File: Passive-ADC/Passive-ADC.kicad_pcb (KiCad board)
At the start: 4 copper layers, 24.2 x 16.8 mm, 13 parts, among them J1 FPGA Terminal, J2 ADC Terminal

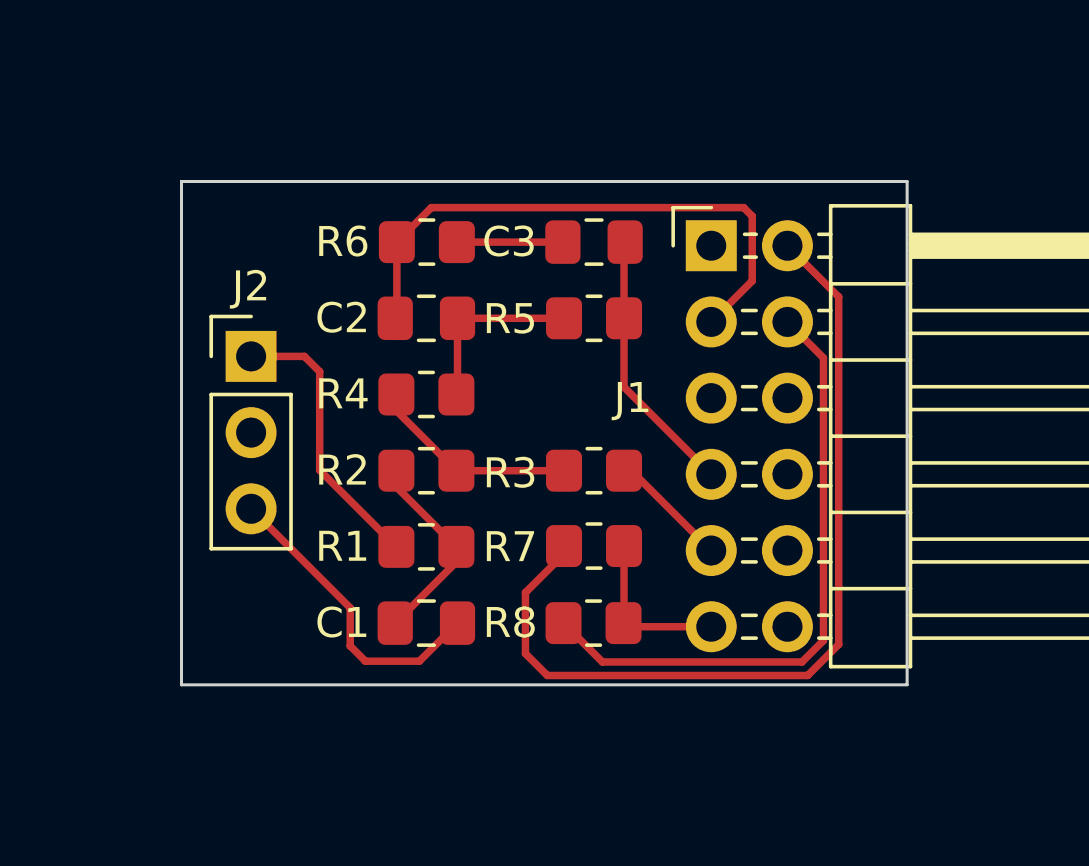
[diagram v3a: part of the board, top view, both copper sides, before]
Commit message: Updated models with new schematic details
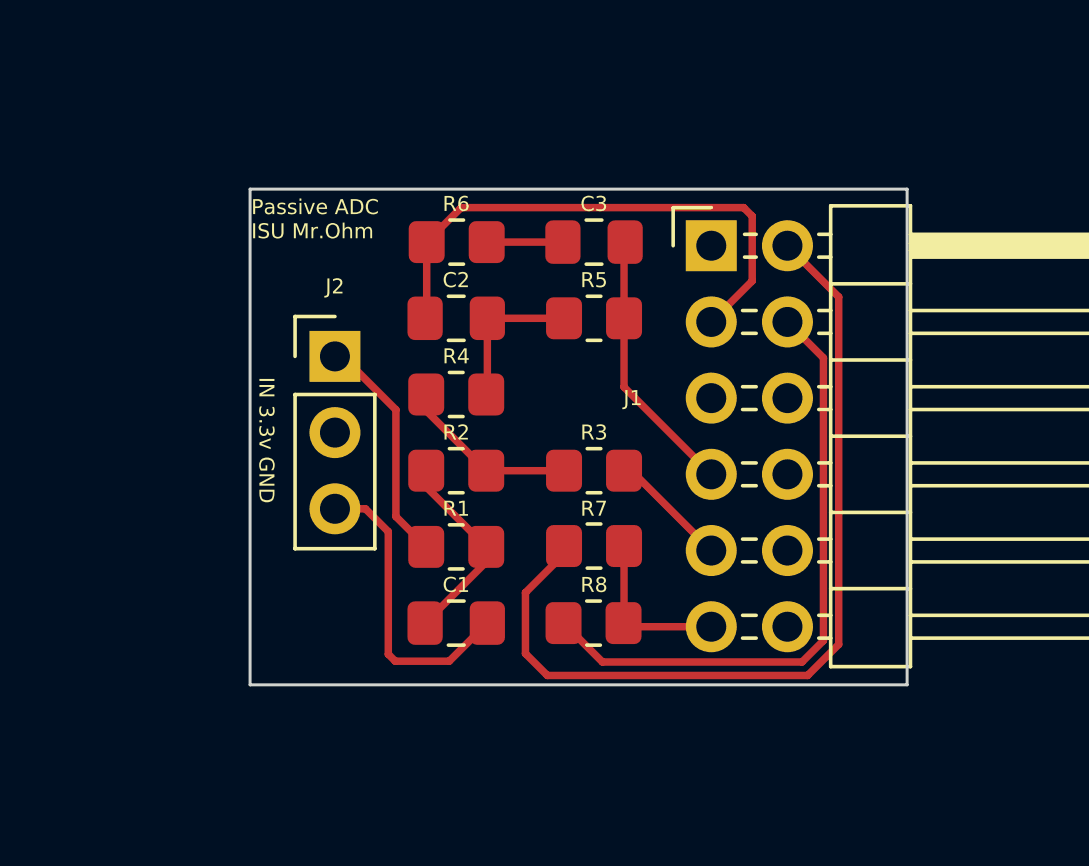
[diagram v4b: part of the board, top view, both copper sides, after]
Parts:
- moved J2 2.79 mm to (144.0, 80.5)
- moved R6 0.99 mm to (148.1, 76.7)
- moved C1 0.99 mm to (148.1, 89.4)
- moved C2 0.99 mm to (148.1, 79.2)
- moved R1 0.99 mm to (148.1, 86.9)
- moved R2 0.99 mm to (148.1, 84.3)
- moved R4 0.99 mm to (148.1, 81.8)
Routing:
- net /Sensor-IN: track 9.40 -> 7.76 mm
- net GND: track 50.0 -> 48.8 mm
- net Net-(C3-Pad2): track 3.56 -> 2.54 mm
- net Net-(C2-Pad1): track 6.11 -> 5.11 mm
- net Net-(R2-Pad2): track 6.96 -> 5.96 mm
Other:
- board size 24.2 x 16.8 mm -> 21.9 x 16.5 mm
- board text added: "IN 3.3v GND"
- board text added: "Passive ADC ISU Mr.Ohm"
